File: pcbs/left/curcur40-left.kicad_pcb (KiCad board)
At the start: 2 copper layers, 124.3 x 91.8 mm, 79 parts, among them J1 TYPE-C-31-M-13C, J2 TRS, J4 Conn_01x03, SW1 SW_Push, SW10 SW_Push, SW11 SW_Push, SW12 SW_Push, SW13 SW_Push, SW14 SW_Push, SW15 SW_Push, SW16 SW_Push, SW17 SW_Push, SW18 SW_Push, SW2 SW_Push, SW3 SW_Push, SW4 SW_Push, SW5 SW_Push, SW6 SW_Push, SW7 SW_Push, SW8 SW_Push, SW9 SW_Push, U1 RP2040, U2 NCP1117LPST33T3G, U3 TPD4E05U06DQAR, U4 W25Q128JVSIQ, Y1 12MHz 18pF

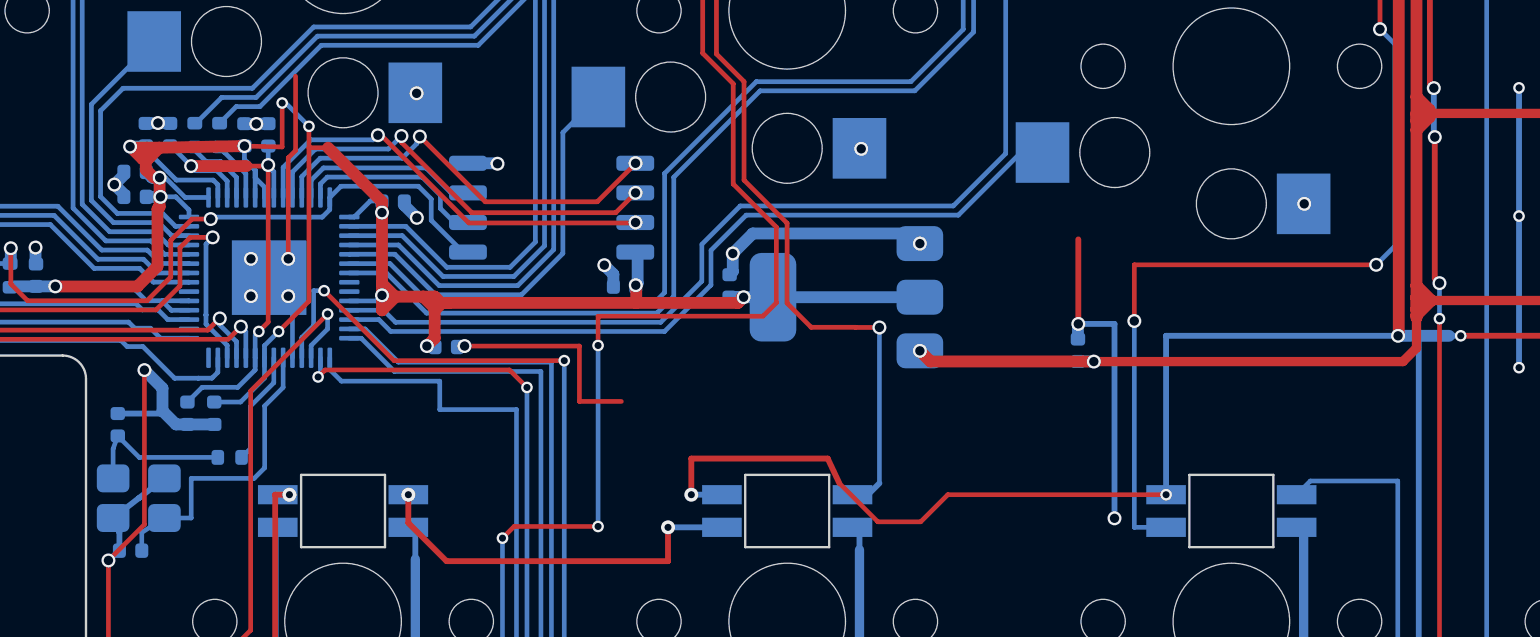
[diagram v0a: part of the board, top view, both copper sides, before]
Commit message: fix(pcb): resolve 0.060mm same-net +3V3 trace spacing at U1 top-left and LED1.4 slot on left PCB
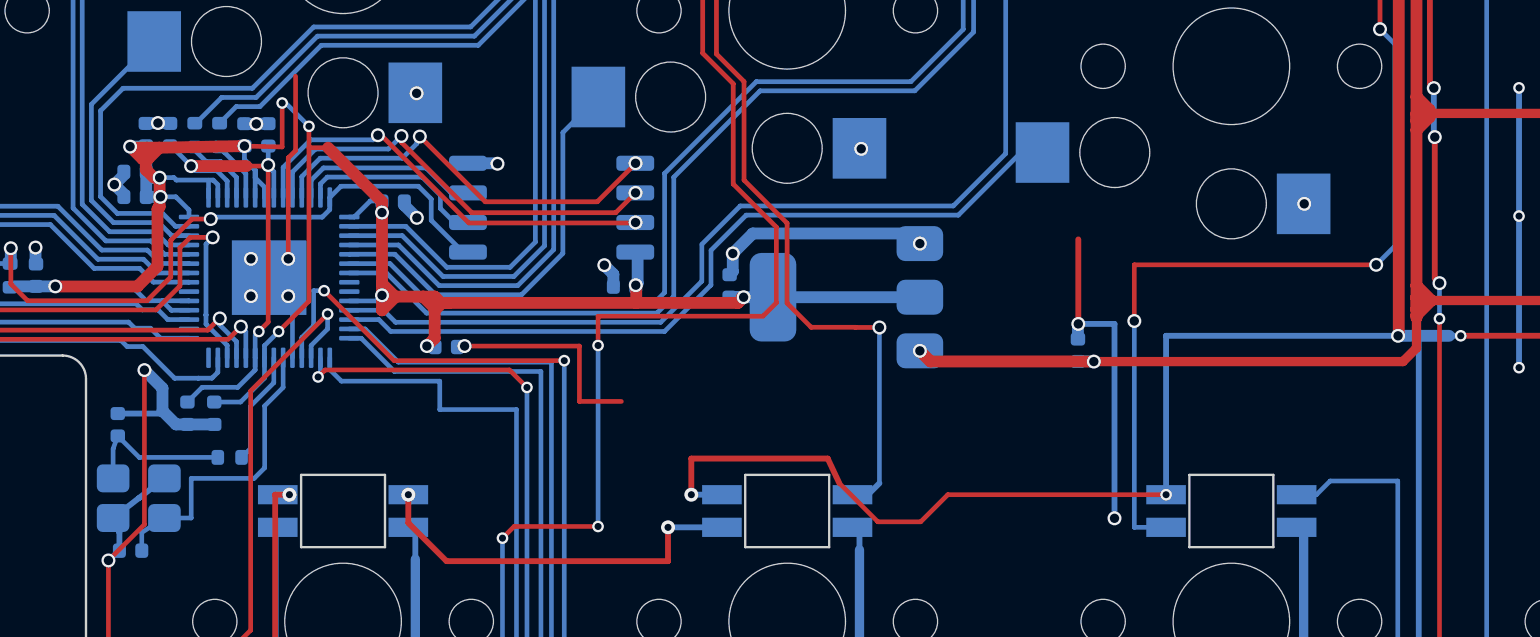
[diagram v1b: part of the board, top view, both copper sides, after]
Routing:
- net +3V3: track 104.4 -> 103.8 mm
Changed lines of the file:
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@@
-	)
-	(segment
-		(start -78.210048 34.20245)
-		(end -77.2075 34.20245)
-		(width 0.2032)
-		(layer "B.Cu")
-		(net "+3V3")
 	)
 	(segment
@@
 	)
 	(segment
+		(start -79.3058 33.3507)
+		(end -78.6917 33.3507)
+		(width 0.2032)
+		(layer "B.Cu")
+		(net "+3V3")
+	)
+	(segment
 		(start -78.60995 34.175)
 		(end -78.045 34.73995)
@@
 	)
 	(segment
-		(start -78.5862 33.45625)
-		(end -77.004768 33.45625)
-		(width 0.2032)
-		(layer "B.Cu")
-		(net "+3V3")
-	)
-	(segment
 		(start -67.8425 40.5745)
 		(end -67.53425 40.5745)
@@
 	)
 	(segment
-		(start -79.305762 33.35066)
-		(end -79.061838 33.35066)
-		(width 0.2032)
-		(layer "B.Cu")
-		(net "+3V3")
-	)
-	(segment
 		(start -58.8025 37.885)
 		(end -58.8825 37.965)
@@
 	)
 	(segment
-		(start -79.8975 32.14495)
-		(end -78.5862 33.45625)
-		(width 0.2032)
-		(layer "B.Cu")
-		(net "+3V3")
-	)
-	(segment
 		(start -74.8075 41.95)
 		(end -75.8338 42.9763)
@@
 	)
 	(segment
+		(start -79.8775 32.0062)
+		(end -79.8775 33.104999)
+		(width 0.508)
+		(layer "B.Cu")
+		(net "+3V3")
+	)
+	(segment
 		(start -79.631838 33.35066)
 		(end -79.877498 33.105)
@@
 	)
 	(segment
+		(start -79.8775 33.104999)
+		(end -79.8775 34.175)
+		(width 0.508)
+		(layer "B.Cu")
+		(net "+3V3")
+	)
+	(segment
 		(start -80.484374 38.0306)
 		(end -79.884324 38.63065)
@@
 	)
 	(segment
+		(start -77.2075 34.2024)
+		(end -77.2075 33.4562)
+		(width 0.2)
+		(layer "B.Cu")
+		(net "+3V3")
+	)
+	(segment
 		(start -75.6675 32.569246)
 		(end -75.6675 31.99625)
@@
 	)
 	(segment
-		(start -79.061838 33.35066)
-		(end -78.210048 34.20245)
-		(width 0.2032)
-		(layer "B.Cu")
-		(net "+3V3")
-	)
-	(segment
 		(start -78.045 34.73995)
 		(end -78.045 35.03995)
@@
 	)
 	(segment
-		(start -76.8075 33.653518)
-		(end -76.8075 34.20245)
-		(width 0.2032)
-		(layer "B.Cu")
-		(net "+3V3")
-	)
-	(segment
 		(start -71.17 35.03995)
 		(end -70.9575 35.03995)
@@
 	)
 	(segment
+		(start -78.5862 33.4562)
+		(end -77.0048 33.4562)
+		(width 0.2032)
+		(layer "B.Cu")
+		(net "+3V3")
+	)
+	(segment
 		(start -75.2075 33.029246)
 		(end -75.2075 34.20245)
@@
 	)
 	(segment
+		(start -78.6917 33.3507)
+		(end -78.5862 33.4562)
+		(width 0.2032)
+		(layer "B.Cu")
+		(net "+3V3")
+	)
+	(segment
 		(start -75.2075 33.35495)
 		(end -75.2075 33.029246)
@@
 		(start -79.305762 33.35066)
 		(end -79.631838 33.35066)
+		(width 0.508)
+		(layer "B.Cu")
+		(net "+3V3")
+	)
+	(segment
+		(start -76.8075 34.2024)
+		(end -76.8075 33.6535)
+		(width 0.2)
+		(layer "B.Cu")
+		(net "+3V3")
+	)
+	(segment
+		(start -79.8975 31.9862)
+		(end -79.8775 32.0062)
 		(width 0.508)
 		(layer "B.Cu")
@@
 	)
 	(segment
+		(start -29.1 46.3625)
+		(end -29.6875 46.95)
+		(width 0.2)
+		(layer "B.Cu")
+		(net "/LED")
+	)
+	(segment
 		(start -26.2 60.1625)
 		(end -26.2 46.3625)
@@
 	)
 	(segment
-		(start -29.95 46.3625)
+		(start -29.6875 46.95)
 		(end -30.5375 46.95)
 		(width 0.2)
@@
 	(segment
 		(start -26.2 46.3625)
-		(end -29.95 46.3625)
-		(width 0.2)
-		(layer "B.Cu")
+		(end -29.1 46.3625)
+		(width 0.2)
+		(layer "B.Cu")

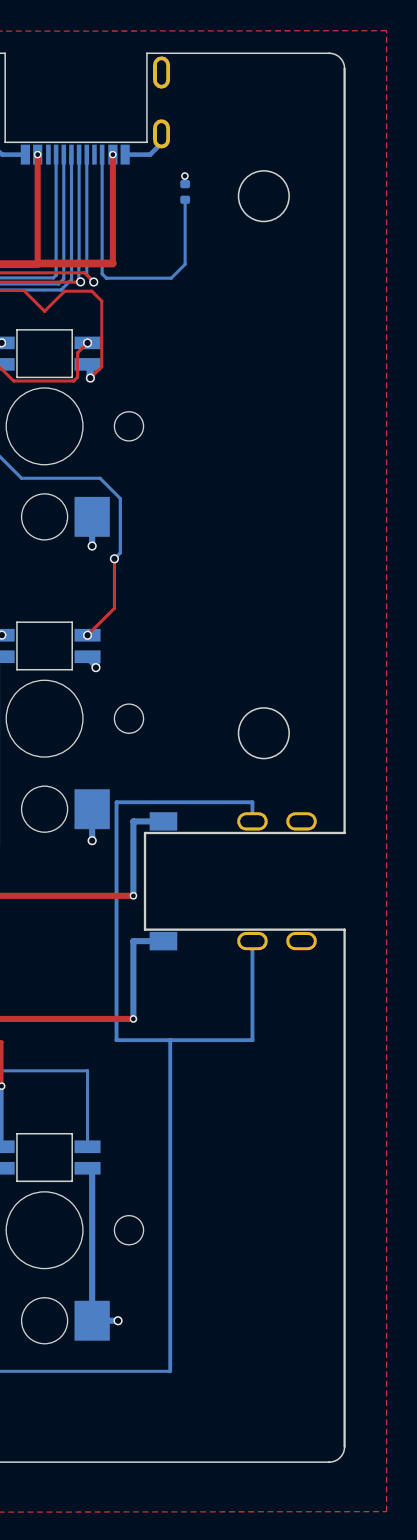
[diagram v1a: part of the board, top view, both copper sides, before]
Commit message: feat(pcb): replace split TRRS jack with USB-C receptacle and ESD/series protection
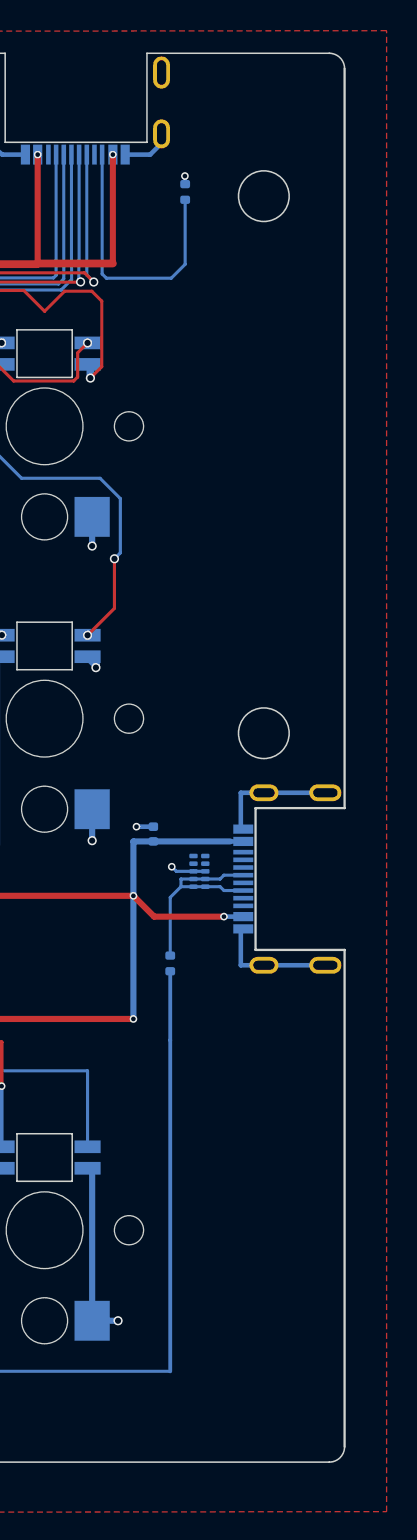
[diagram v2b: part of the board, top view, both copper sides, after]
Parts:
- added C17: 100n, Capacitor_SMD:C_0402_1005Metric, B.Cu at (-7.20, 26.6)
- added R10: 27, Resistor_SMD:R_0402_1005Metric, B.Cu at (-6.10, 35.0)
- added U5: TPD4E05U06DQAR, Package_SON:USON-10_2.5x1.0mm_P0.5mm, B.Cu at (-4.20, 29.0)
- J2: value TRS -> TYPE-C-31-M-13C; footprint kbd:Jack_PJ-398A-5A_PJ-399B-6A -> kbd:USB_C_Receptacle_TYPE-C-31-M-13C
- moved J2 1.26 mm to (4.01, 29.5), turned to -90 degrees
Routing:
- net /TX: track 149.3 -> 112.8 mm
- net GND: track 210.6 -> 229.9 mm, vias 65 -> 67
- net /SPLIT_DP: track 0.00 -> 13.6 mm
- net +5V: track 139.7 -> 152.3 mm, vias 6 -> 7
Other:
- outline, holes or cut-outs redrawn
